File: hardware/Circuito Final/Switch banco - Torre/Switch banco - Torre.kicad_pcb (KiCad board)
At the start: 2 copper layers, 13 parts, among them J3 Conn_01x06_Socket, Q1_1 MMBT2222A, Q3 MMBT2222A, U1 74HC595

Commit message: sube conexion del shift register en el banco
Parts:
- removed J_der1: Conn_02x06_Odd_Even, Connector_PinSocket_2.54mm:PinSocket_2x06_P2.54mm_Vertical
- removed R1_8: 330k, Resistor_SMD:R_1206_3216Metric_Pad1.30x1.75mm_HandSolder
- removed R1_9: 20k, Resistor_SMD:R_1206_3216Metric_Pad1.30x1.75mm_HandSolder
- added H1: MountingHole, MountingHole:MountingHole_3.5mm, F.Cu at (102.8, 87.0)
- added H2: MountingHole, MountingHole:MountingHole_3.5mm, F.Cu at (196.0, 87.0)
- added H3: MountingHole, MountingHole:MountingHole_3.5mm, F.Cu at (102.8, 119.6)
- added H4: MountingHole, MountingHole:MountingHole_3.5mm, F.Cu at (196.0, 119.6)
- added J1: Conn_01x07_Socket, Connector_PinSocket_2.54mm:PinSocket_1x07_P2.54mm_Vertical, F.Cu at (125.8, 116.5)
- added J2: Conn_01x13_Socket, Connector_PinSocket_2.54mm:PinSocket_1x13_P2.54mm_Vertical, F.Cu at (136.3, 116.4)
- added R1_0: 33k, Resistor_SMD:R_1206_3216Metric_Pad1.30x1.75mm_HandSolder, B.Cu at (168.6, 58.0)
- added R1_1: 33k, Resistor_SMD:R_1206_3216Metric_Pad1.30x1.75mm_HandSolder, B.Cu at (168.6, 54.6)
- added R1_2: 33k, Resistor_SMD:R_1206_3216Metric_Pad1.30x1.75mm_HandSolder, B.Cu at (168.6, 51.3)
- added R1_3: 33k, Resistor_SMD:R_1206_3216Metric_Pad1.30x1.75mm_HandSolder, B.Cu at (168.6, 48.0)
- added R1_4: 33k, Resistor_SMD:R_1206_3216Metric_Pad1.30x1.75mm_HandSolder, B.Cu at (184.8, 96.2)
- added R1_5: 33k, Resistor_SMD:R_1206_3216Metric_Pad1.30x1.75mm_HandSolder, B.Cu at (184.8, 93.3)
- added R1_6: 33k, Resistor_SMD:R_1206_3216Metric_Pad1.30x1.75mm_HandSolder, B.Cu at (184.8, 90.3)
- added R2_0: 8.2k, Resistor_SMD:R_1206_3216Metric_Pad1.30x1.75mm_HandSolder, B.Cu at (180.4, 56.1)
- added R2_1: 8.2k, Resistor_SMD:R_1206_3216Metric_Pad1.30x1.75mm_HandSolder, B.Cu at (174.6, 54.6)
- added R2_2: 8.2k, Resistor_SMD:R_1206_3216Metric_Pad1.30x1.75mm_HandSolder, B.Cu at (174.6, 51.3)
- added R2_3: 8.2k, Resistor_SMD:R_1206_3216Metric_Pad1.30x1.75mm_HandSolder, B.Cu at (174.6, 48.0)
- added R2_4: 8.2k, Resistor_SMD:R_1206_3216Metric_Pad1.30x1.75mm_HandSolder, B.Cu at (168.4, 80.7)
- added R2_5: 8.2k, Resistor_SMD:R_1206_3216Metric_Pad1.30x1.75mm_HandSolder, B.Cu at (172.5, 99.4)
- added R2_6: 8.2k, Resistor_SMD:R_1206_3216Metric_Pad1.30x1.75mm_HandSolder, B.Cu at (170.7, 87.3)
- added R2_7: 8.2k, Resistor_SMD:R_1206_3216Metric_Pad1.30x1.75mm_HandSolder, B.Cu at (167.1, 92.4)
- added R7: 570k, Resistor_SMD:R_1206_3216Metric_Pad1.30x1.75mm_HandSolder, B.Cu at (85.1, 79.3)
- added R8: 330k, Resistor_SMD:R_1206_3216Metric_Pad1.30x1.75mm_HandSolder, B.Cu at (90.6, 79.3)
- added R9: 20k, Resistor_SMD:R_1206_3216Metric_Pad1.30x1.75mm_HandSolder, B.Cu at (119.1, 56.5)
- added Rp1: 10k, Resistor_SMD:R_1206_3216Metric_Pad1.30x1.75mm_HandSolder, B.Cu at (129.3, 81.9)
- added Rp2: 10k, Resistor_SMD:R_1206_3216Metric_Pad1.30x1.75mm_HandSolder, B.Cu at (137.5, 99.1)
- added Rp3: 10k, Resistor_SMD:R_1206_3216Metric_Pad1.30x1.75mm_HandSolder, B.Cu at (137.5, 102.7)
- added Rp4: 10k, Resistor_SMD:R_1206_3216Metric_Pad1.30x1.75mm_HandSolder, B.Cu at (137.5, 106.2)
- added Rp5: 10k, Resistor_SMD:R_1206_3216Metric_Pad1.30x1.75mm_HandSolder, B.Cu at (126.0, 102.8)
- added Rp6: 10k, Resistor_SMD:R_1206_3216Metric_Pad1.30x1.75mm_HandSolder, B.Cu at (126.0, 99.2)
- added Rp7: 10k, Resistor_SMD:R_1206_3216Metric_Pad1.30x1.75mm_HandSolder, B.Cu at (114.0, 103.3)
- added Rp8: 10k, Resistor_SMD:R_1206_3216Metric_Pad1.30x1.75mm_HandSolder, B.Cu at (114.1, 99.7)
- added Rp9: 10k, Resistor_SMD:R_1206_3216Metric_Pad1.30x1.75mm_HandSolder, B.Cu at (112.8, 91.4)
- added Rs0: 330, Resistor_SMD:R_1206_3216Metric_Pad1.30x1.75mm_HandSolder, B.Cu at (129.3, 78.9)
- added Rs1: 330, Resistor_SMD:R_1206_3216Metric_Pad1.30x1.75mm_HandSolder, B.Cu at (129.8, 110.1)
- added Rs2: 330, Resistor_SMD:R_1206_3216Metric_Pad1.30x1.75mm_HandSolder, B.Cu at (126.6, 110.1)
- added Rs3: 330, Resistor_SMD:R_1206_3216Metric_Pad1.30x1.75mm_HandSolder, B.Cu at (123.4, 110.1)
- added Rs4: 330, Resistor_SMD:R_1206_3216Metric_Pad1.30x1.75mm_HandSolder, B.Cu at (120.1, 110.1)
- added Rs5: 330, Resistor_SMD:R_1206_3216Metric_Pad1.30x1.75mm_HandSolder, B.Cu at (116.9, 110.1)
- added Rs6: 330, Resistor_SMD:R_1206_3216Metric_Pad1.30x1.75mm_HandSolder, B.Cu at (113.7, 110.1)
- added Rs7: 330, Resistor_SMD:R_1206_3216Metric_Pad1.30x1.75mm_HandSolder, B.Cu at (110.4, 110.1)
- added U2: 74HC4051, Package_DIP:DIP-16_W7.62mm_SMDSocket_SmallPads, B.Cu at (159.7, 91.1)
- D1: footprint LED_THT:LED_D1.8mm_W1.8mm_H2.4mm_Horizontal_O1.27mm_Z1.6mm -> LED_THT:LED_D5.0mm
- J3: value Conn_01x06_Socket -> Conn_02x07_Odd_Even; footprint Connector_PinSocket_2.54mm:PinSocket_1x06_P2.54mm_Vertical -> Connector_PinSocket_2.54mm:PinSocket_1x07_P2.54mm_Vertical
- J_izq1: value Conn_02x06_Odd_Even -> Conn_02x04_Odd_Even; footprint Connector_PinSocket_2.54mm:PinSocket_2x06_P2.54mm_Vertical -> Connector_PinSocket_2.54mm:PinSocket_1x04_P2.54mm_Vertical
- Q1_1, Q3, R4, R5, S1, U1: moved to B.Cu
- R1_7: value 570k -> 33k; moved to B.Cu
- moved J3 344.5 mm to (190.1, 106.0), turned to 180 degrees
- moved Q3 303.5 mm to (111.3, 82.2), turned to -90 degrees
- moved U1 294.4 mm to (125.5, 91.0), turned to 90 degrees
- moved R1_7 288.9 mm to (140.5, 50.0)
- moved Q1_1 275.5 mm to (113.5, 58.2), turned to 180 degrees
- moved D1 271.5 mm to (105.7, 92.8), turned to -90 degrees
- moved J_izq1 268.1 mm to (105.7, 107.1), turned to 180 degrees
- moved R5 266.1 mm to (109.7, 86.3)
- moved R4 263.6 mm to (107.4, 81.5), turned to -90 degrees
- moved S1 249.7 mm to (85.0, 74.7), turned to 90 degrees
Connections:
- J3 pad 1: /Vcell1 -> /cell_neg1
- J3 pad 2: /Vcell2 -> /cell_neg2
- J3 pad 3: /Vcell3 -> /cell_neg3
- J3 pad 4: /Vcell4 -> /cell_neg4
- J3 pad 5: /Vcell5 -> /cell_neg5
- J3 pad 6: /Vcell6 -> /cell_neg6
- J_izq1 pad 2: /bus_neg -> GND
- J_izq1 pad 3: GND -> /bus_pos
- J_izq1 pad 4: GND -> /Vcc
- R1_7 pad 1: /bus_pos -> Net-(U2-A7)
- R1_7 pad 2: Net-(S1-G) -> /bus_pos
- R4 pad 1: /v_control -> /Vbanco
- U1 pad 1: /Vcell1 -> Net-(U1-QB)
- U1 pad 10: unconnected-(U1-~{SRCLR}-Pad10) -> /reset
- U1 pad 11: unconnected-(U1-SRCLK-Pad11) -> /clock
- U1 pad 12: unconnected-(U1-RCLK-Pad12) -> /latch
- U1 pad 13: unconnected-(U1-~{OE}-Pad13) -> /MASTER
- U1 pad 14: unconnected-(U1-SER-Pad14) -> /DATA
- U1 pad 15: unconnected-(U1-QA-Pad15) -> Net-(U1-QA)
- U1 pad 16: unconnected-(U1-VCC-Pad16) -> /Vcc
- U1 pad 2: /Vcell2 -> Net-(U1-QC)
- U1 pad 3: /Vcell3 -> Net-(U1-QD)
- U1 pad 4: /Vcell4 -> Net-(U1-QE)
- U1 pad 5: /Vcell5 -> Net-(U1-QF)
- U1 pad 6: /Vcell6 -> Net-(U1-QG)
- U1 pad 7: unconnected-(U1-QH-Pad7) -> Net-(U1-QH)
- U1 pad 8: unconnected-(U1-GND-Pad8) -> GND
- U1 pad 9: unconnected-(U1-QH'-Pad9) -> Net-(U1-QH')
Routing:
- net GND: track 0.00 -> 94.7 mm
- net /DATA: track 0.00 -> 60.9 mm
- net /reset: track 0.00 -> 46.5 mm
- net /clock: track 0.00 -> 45.1 mm
- net /latch: track 0.00 -> 44.5 mm
- net /MASTER: track 0.00 -> 44.3 mm
- net /salida_adc: track 0.00 -> 32.5 mm
- net Net-(U1-QB): track 0.00 -> 29.5 mm
- net Net-(U1-QD): track 0.00 -> 29.1 mm
- net Net-(U1-QC): track 0.00 -> 28.2 mm
- net Net-(U1-QH): track 0.00 -> 19.0 mm
- net Net-(U1-QG): track 0.00 -> 16.5 mm
- net Net-(U1-QF): track 0.00 -> 16.3 mm
- net Net-(U1-QE): track 0.00 -> 15.9 mm
- net Net-(U2-A5): track 0.00 -> 15.0 mm
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
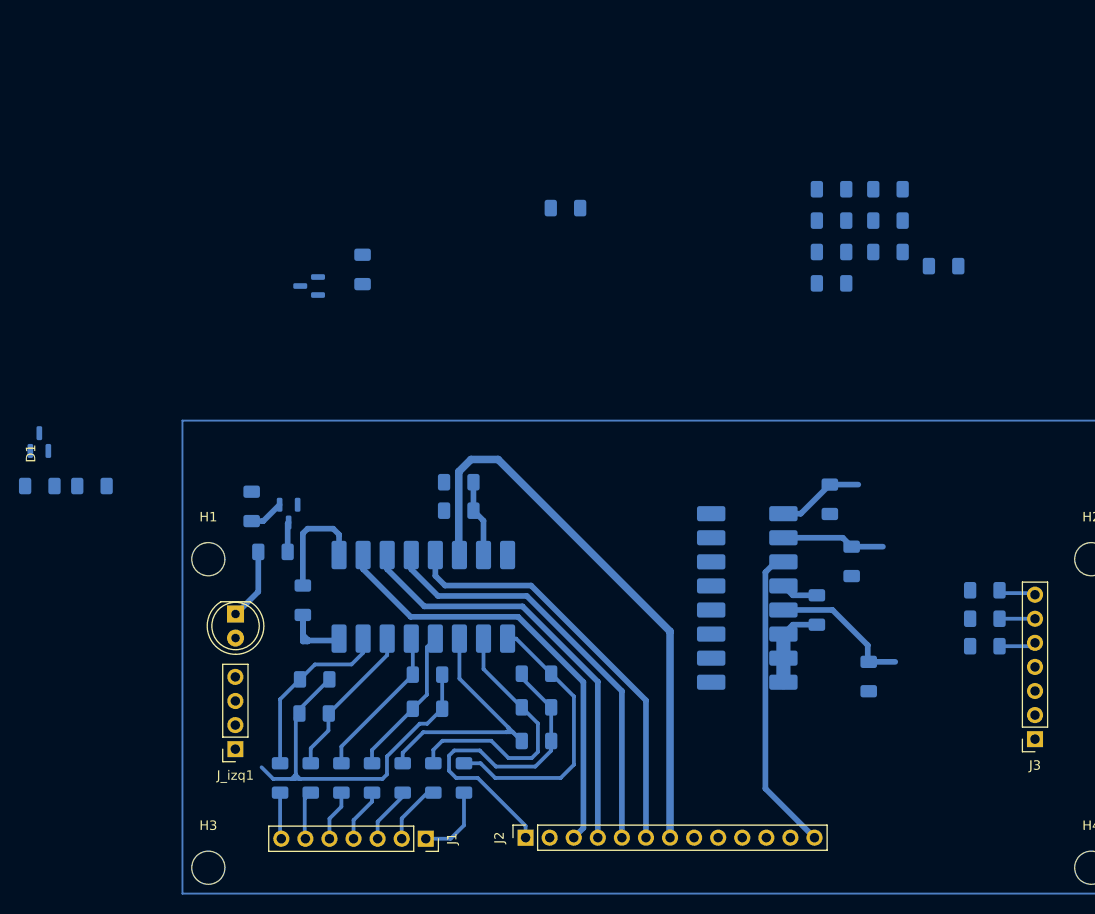
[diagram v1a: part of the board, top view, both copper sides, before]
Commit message: conecta los integrados en el pcb del banco
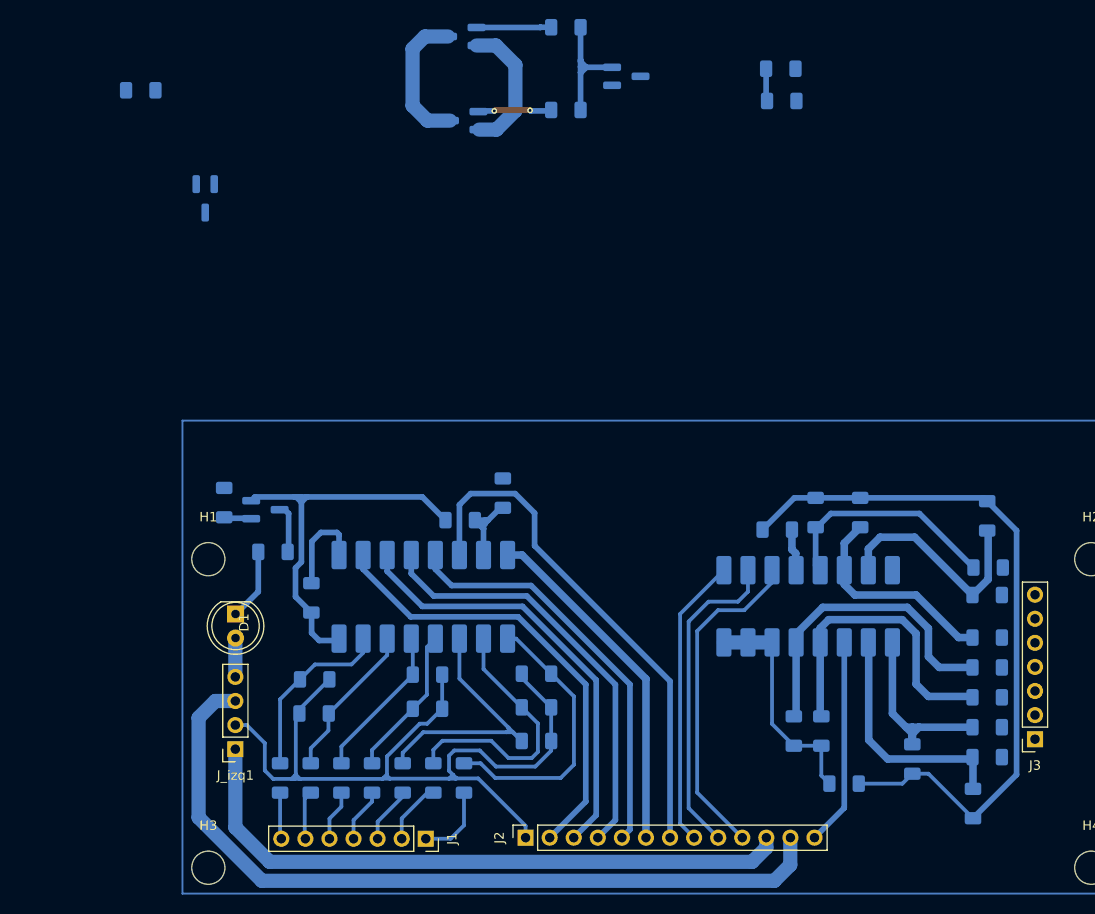
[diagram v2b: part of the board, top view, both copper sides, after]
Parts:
- removed R1_3: 33k, Resistor_SMD:R_1206_3216Metric_Pad1.30x1.75mm_HandSolder
- added Q1: MMBFJ112, Package_TO_SOT_SMD:SOT-23_Handsoldering, B.Cu at (146.9, 36.1)
- added R2_8: 0, Resistor_SMD:R_1206_3216Metric_Pad1.30x1.75mm_HandSolder, B.Cu at (169.9, 110.7)
- added Rg1: 3, Resistor_SMD:R_1206_3216Metric_Pad1.30x1.75mm_HandSolder, B.Cu at (140.6, 39.7)
- added Rg2: 3, Resistor_SMD:R_1206_3216Metric_Pad1.30x1.75mm_HandSolder, B.Cu at (140.6, 30.9)
- added S2: IRLML6402, Package_TO_SOT_SMD:SOT-23_Handsoldering, B.Cu at (129.8, 40.8)
- H1, H2, H3, H4: footprint MountingHole:MountingHole_3.5mm -> modificados:MountingHole_3.5mm
- Q1_1, Q3, S1: footprint Package_TO_SOT_SMD:SOT-23 -> Package_TO_SOT_SMD:SOT-23_Handsoldering
- moved R7 88.2 mm to (163.3, 38.7), turned to 180 degrees
- moved R8 85.0 mm to (163.2, 35.3)
- moved R1_7 68.1 mm to (185.0, 101.6)
- moved S1 61.8 mm to (129.6, 31.9), turned to 180 degrees
- moved R1_1 43.9 mm to (185.0, 95.3)
- moved R1_2 42.8 mm to (185.0, 90.8)
- moved R2_3 37.8 mm to (162.9, 83.9), turned to 180 degrees
- moved R1_0 34.2 mm to (185.1, 87.9)
- moved R2_2 32.9 mm to (185.0, 82.5), turned to 90 degrees
- moved R9 30.1 mm to (95.7, 37.6), turned to 0 degrees
- moved R2_0 29.3 mm to (166.9, 82.1), turned to 90 degrees
- moved R2_4 28.7 mm to (177.1, 108.1)
- moved R2_6 28.6 mm to (183.5, 112.8)
- moved R2_1 27.6 mm to (171.6, 82.1), turned to 90 degrees
- moved R1_6 17.6 mm to (185.0, 107.9)
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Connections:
- J2 pad 10: /Bit_2 -> /Bit_0
- J2 pad 2: /Vcc -> /reset
- J2 pad 3: /reset -> /clock
- J2 pad 4: /clock -> /latch
- J2 pad 5: /latch -> /MASTER
- J2 pad 6: /MASTER -> /Vcc
- J2 pad 8: /Bit_0 -> /Bit_2
- R1_0 pad 2: /cell_neg1 -> /cell_neg7
- R1_1 pad 2: /cell_neg2 -> /cell_neg5
- R1_2 pad 2: /cell_neg3 -> /cell_neg6
- R1_4 pad 2: /cell_neg5 -> /cell_neg2
- R1_5 pad 2: /cell_neg6 -> /cell_neg4
- R1_6 pad 2: /cell_neg7 -> /cell_neg1
- R1_7 pad 2: /bus_pos -> /cell_neg3
- R7 pad 2: Net-(S1-G) -> Net-(Q1-S)
- R8 pad 1: Net-(S1-G) -> Net-(Q1-S)
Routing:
- net GND: track 94.7 -> 234.0 mm
- net /bus_pos: track 0.00 -> 98.3 mm
- net /bus_neg: track 0.00 -> 82.3 mm
- net /Vcc: track 0.00 -> 40.9 mm
- net /Bit_0: track 0.00 -> 35.1 mm
- net /Bit_1: track 0.00 -> 33.9 mm
- net /Bit_2: track 0.00 -> 30.7 mm
- net Net-(U2-A7): track 3.94 -> 32.3 mm
- net Net-(U2-A0): track 0.00 -> 24.3 mm
- net Net-(U2-A2): track 0.00 -> 23.8 mm
- net Net-(U2-A1): track 0.00 -> 22.6 mm
- net Net-(U2-A5): track 15.0 -> 32.9 mm
- net Net-(Q1-S): track 0.00 -> 17.4 mm
- net Net-(U2-A6): track 10.9 -> 25.5 mm
- net Net-(U2-A4): track 9.17 -> 22.5 mm
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
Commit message: sube pcb del banco todo conectado
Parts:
- added F1: Fuse, Fuse:Fuse_1206_3216Metric_Pad1.42x1.75mm_HandSolder, B.Cu at (148.0, 95.6)
- added R2_10: 0, Resistor_SMD:R_1206_3216Metric_Pad1.30x1.75mm_HandSolder, B.Cu at (141.8, 78.4)
- added R2_9: 0, Resistor_SMD:R_1206_3216Metric_Pad1.30x1.75mm_HandSolder, B.Cu at (194.7, 82.1)
- added TP1: TestPoint, TestPoint:TestPoint_Loop_D2.54mm_Drill1.5mm_Beaded, F.Cu at (190.0, 82.0)
- J1: value Conn_01x07_Socket -> Conn_01x07
- J2: value Conn_01x13_Socket -> Conn_02x07_Odd_Even; footprint Connector_PinSocket_2.54mm:PinSocket_1x13_P2.54mm_Vertical -> Connector_IDC:IDC-Header_2x07_P2.54mm_Horizontal
- J3: value Conn_02x07_Odd_Even -> Conn_01x07
- J_izq1: value Conn_02x04_Odd_Even -> Conn_01x04
- Rg1, Rg2: value 3 -> 100
- moved Q1_1 79.4 mm to (174.7, 82.0)
- moved R9 64.9 mm to (141.8, 83.3)
- moved Rg1 55.2 mm to (160.1, 91.2)
- moved Rg2 54.9 mm to (160.5, 82.1)
- moved S1 54.3 mm to (149.4, 82.5)
- moved S2 53.1 mm to (149.5, 90.1)
- moved Q1 49.6 mm to (165.2, 82.2), turned to -90 degrees
- moved R7 47.9 mm to (160.5, 86.5), turned to -90 degrees
- moved R8 47.4 mm to (169.6, 82.3), turned to -90 degrees
- moved J2 22.4 mm to (158.6, 114.1), turned to -90 degrees
- moved R4 17.7 mm to (122.2, 81.9), turned to 180 degrees
- moved R2_2 16.5 mm to (169.7, 88.6), turned to 180 degrees
- moved R2_0 14.1 mm to (180.2, 86.9)
- moved R2_1 9.62 mm to (169.6, 91.5), turned to 180 degrees
- moved U2 8.21 mm to (165.9, 100.2)
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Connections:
- J2 pad 1: GND -> /Bit_1
- J2 pad 10: /Bit_0 -> GND
- J2 pad 11: /bus_neg -> /DATA
- J2 pad 12: /bus_pos -> /reset
- J2 pad 13: /salida_adc -> /latch
- J2 pad 2: /reset -> /Bit_0
- J2 pad 3: /clock -> /Bit_2
- J2 pad 4: /latch -> /salida_adc
- J2 pad 5: /MASTER -> /bus_pos
- J2 pad 6: /Vcc -> /bus_pos
- J2 pad 7: /DATA -> /bus_neg
- J2 pad 8: /Bit_2 -> /bus_neg
- J2 pad 9: /Bit_1 -> /Vcc
- S1 pad 3: /bus_neg -> Net-(S1-D)
- S2 pad 3: /bus_neg -> Net-(S1-D)
- U1 pad 13: /MASTER -> GND
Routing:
- net /Vcc: track 40.9 -> 197.2 mm
- net GND: track 234.0 -> 346.4 mm
- net /MASTER: track 43.6 -> 0.00 mm
- net Net-(Q1_1-B): track 0.00 -> 35.0 mm
- net /bus_pos: track 98.3 -> 131.6 mm
- net Net-(Q1-S): track 17.4 -> 40.1 mm
- net /Vbanco: track 0.00 -> 19.1 mm
- net Net-(S1-D): track 0.00 -> 17.3 mm
- net /DATA: track 54.7 -> 38.1 mm
- net /Bit_1: track 33.9 -> 23.7 mm
- net Net-(Q1-G): track 0.00 -> 9.52 mm
- net Net-(U2-A4): track 22.5 -> 13.7 mm
- net Net-(U2-A7): track 32.3 -> 23.9 mm
- net /reset: track 47.8 -> 54.8 mm
- net Net-(Q3-B): track 2.85 -> 9.84 mm
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- added copper zone on B.Cu, net GND
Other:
- board outline added: 98.6 x 49 mm
- board text added: "Balanceitor Banco v2.0"

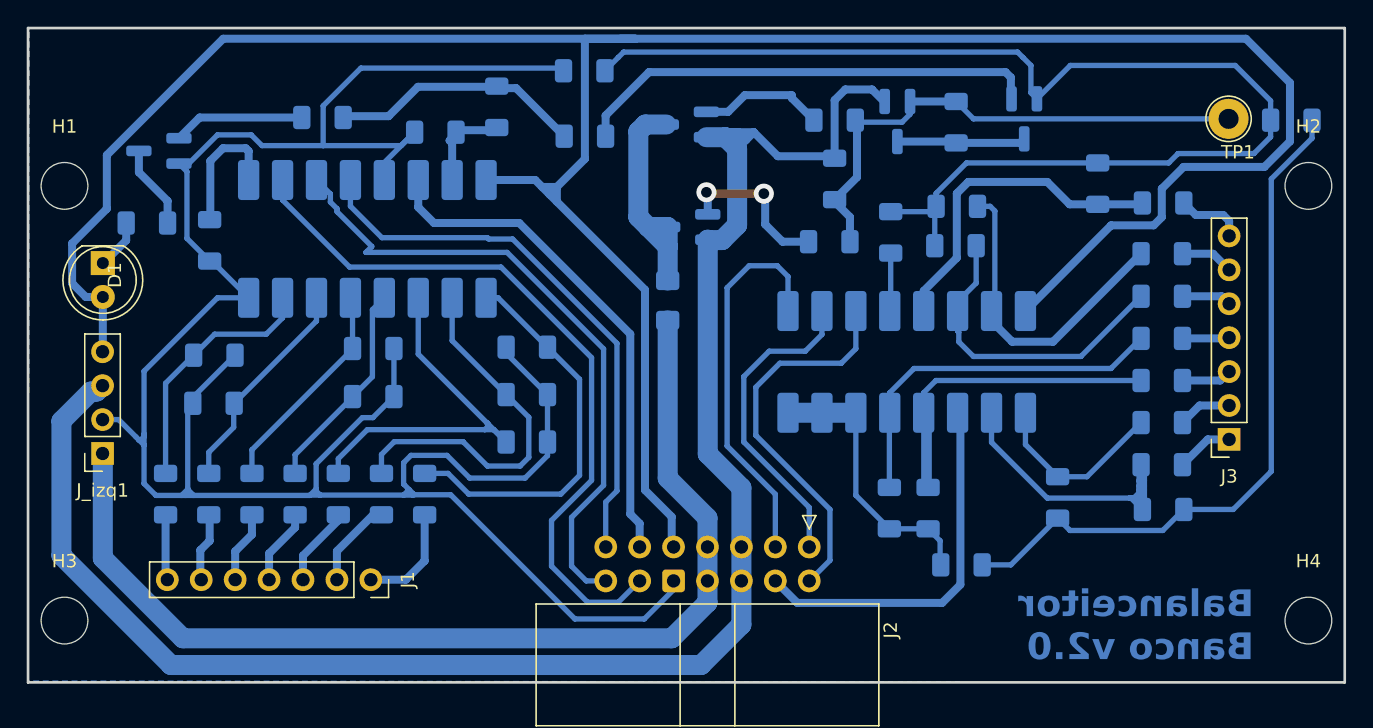
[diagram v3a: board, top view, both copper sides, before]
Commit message: update de valores del codigo y subida de archivos historicos de los PCBs
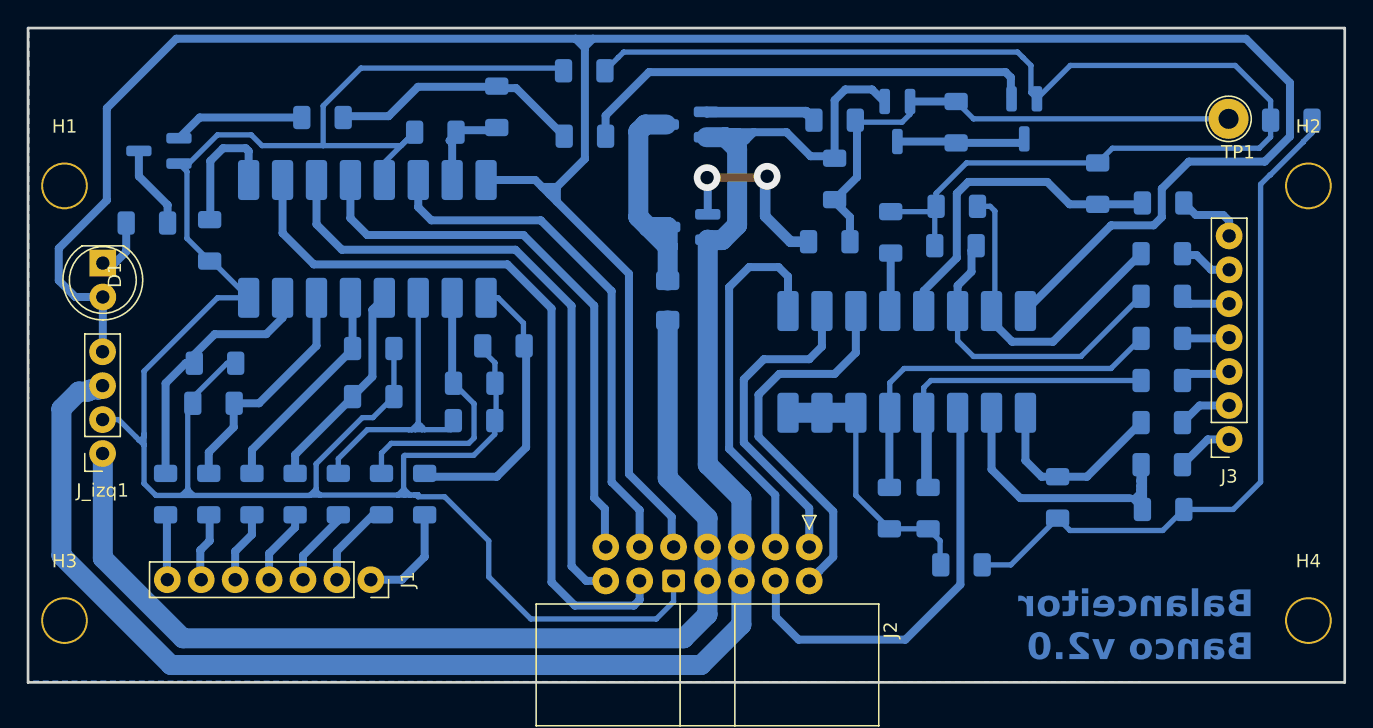
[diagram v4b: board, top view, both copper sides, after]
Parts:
- moved Rp4 4.26 mm to (133.5, 104.6)
- moved Rp3 4.03 mm to (133.5, 101.8)
- moved Rp2 1.75 mm to (135.7, 99.0)
- moved Rp8 0.60 mm to (114.1, 100.3)
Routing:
- net Net-(U1-QB): track 29.5 -> 21.2 mm
- net Net-(U1-QC): track 28.2 -> 20.1 mm
- net Net-(U1-QD): track 29.1 -> 23.2 mm
- net GND: track 346.4 -> 342.3 mm
- net /salida_adc: track 28.1 -> 31.9 mm
- net Net-(S2-G): track 11.7 -> 14.4 mm
- net Net-(U2-A6): track 22.2 -> 23.4 mm
- net Net-(S1-G): track 9.46 -> 8.31 mm
- net /reset: track 54.8 -> 55.9 mm
- net Net-(U1-QG): track 16.5 -> 17.6 mm
- net /DATA: track 38.1 -> 39.2 mm
- net /clock: track 49.0 -> 48.0 mm
- net Net-(U2-A4): track 13.7 -> 14.4 mm
- net /Vcc: track 197.2 -> 196.6 mm
- net /bus_pos: track 131.6 -> 132.1 mm
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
